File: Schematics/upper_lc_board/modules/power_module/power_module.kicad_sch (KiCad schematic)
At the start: 28 parts, among them U3 AMS1117-3.3, U4 ID_LM66100DCKR, U5 ID_LM66100DCKR, U9 TVS3300DRV

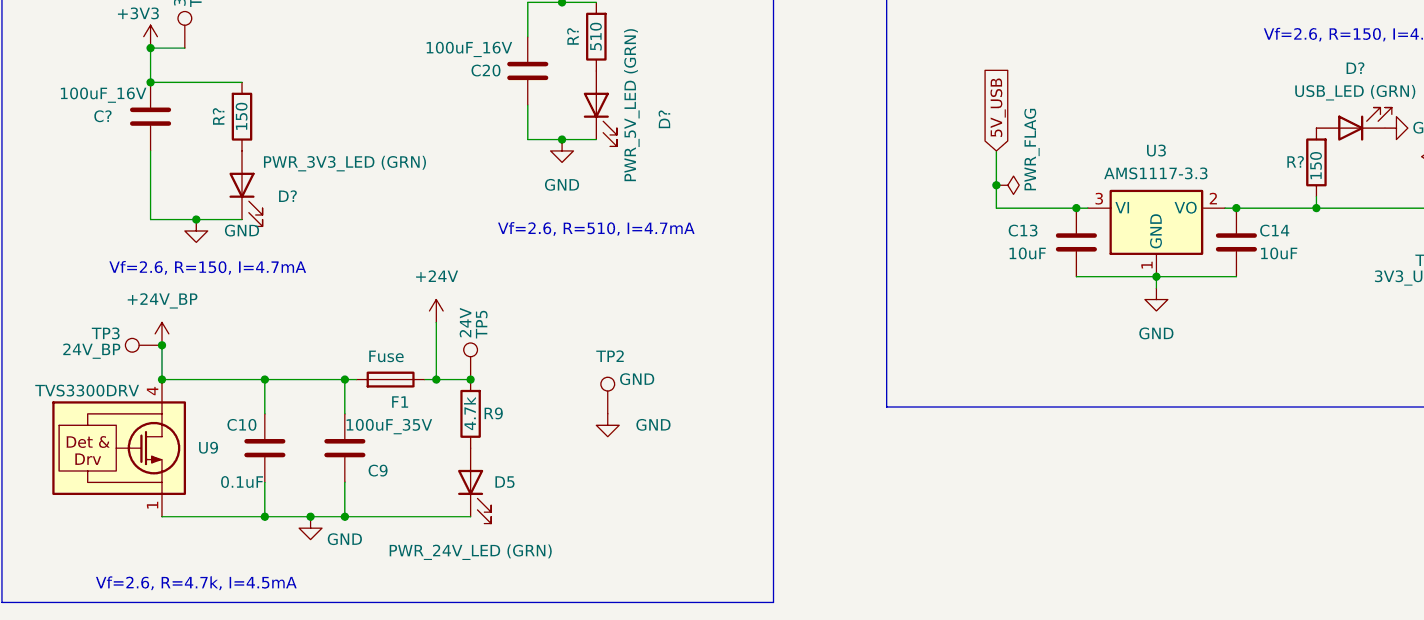
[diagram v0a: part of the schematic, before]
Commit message: add references to caps, ferrite bead footprint, LDO datasheet
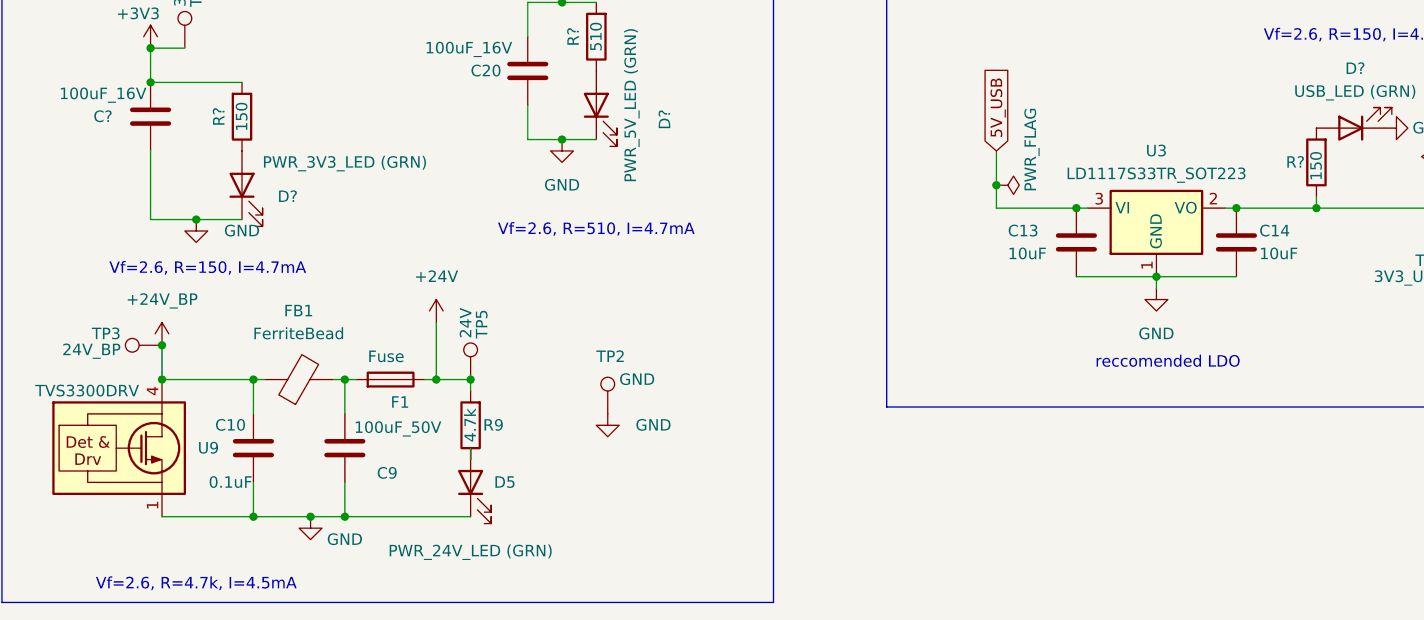
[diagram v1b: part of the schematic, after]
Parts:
- removed U3: AMS1117-3.3, Package_TO_SOT_SMD:SOT-223-3_TabPin2, symbol Regulator_Linear:AMS1117-3.3
- added FB1: FerriteBead, BLM31KN121SN1L:BEADC3216X180N, symbol Device:FerriteBead
- added U3: LD1117S33TR_SOT223, Package_TO_SOT_SMD:SOT-223-3_TabPin2, symbol Regulator_Linear:LD1117S33TR_SOT223
- C9: value 100uF_35V -> 100uF_50V
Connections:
- net +24V_BP: now also FB1.1; no longer C9.1, F1.2
- net 3V3_USB: now also U3.2 (VO)
- net 5V_USB: now also U3.3 (VI)
- net GND: now also U3.1 (GND)
- new net: C9.1, F1.2, FB1.2
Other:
- note added: "reccomended LDO"
- moved on the sheet: C10, R9
